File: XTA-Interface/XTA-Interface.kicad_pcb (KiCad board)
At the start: 2 copper layers, 99.9 x 99.9 mm, 23 parts, among them J1 IDE_CONNECTOR, J2 CF Adapter Power, J3 Bus_ISA_8bit, J4 Addresses, J5 Addresses, U1 BIOS FLASH, U2 74HCT245, U3 ATF/GAL22V10x-15, U4 DS1315, U5 AS6C4008-55PCN, Y1 32.768 KHz

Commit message: WIP on XTA interface card.
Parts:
- removed BAT1: CR2032, Battery:BatteryHolder_Keystone_103_1x20mm
- removed C7: 22uF, Capacitor_THT:CP_Radial_D5.0mm_P2.50mm
- removed H1, H3: MountingHole_Pad, MountingHole:MountingHole_3.5mm_Pad
- removed Y1: 32.768 KHz, Crystal:Crystal_C38-LF_D3.0mm_L8.0mm_Horizontal
- added J6: LEDs, Connector_PinHeader_2.54mm:PinHeader_1x04_P2.54mm_Horizontal, F.Cu at (108.6, 52.7)
- added J7: XTA_CONNECTOR_1, Connector_PinHeader_2.54mm:PinHeader_2x20_P2.54mm_Vertical, F.Cu at (123.8, 60.3)
- added R1: 1K, Resistor_SMD:R_1206_3216Metric, F.Cu at (112.4, 52.1)
- C1, C2, C3, C4, C5: footprint Capacitor_THT:C_Disc_D6.0mm_W2.5mm_P5.00mm -> Capacitor_SMD:C_1206_3216Metric
- C6: value 0.1uF -> 22uF 25v; footprint Capacitor_THT:C_Disc_D6.0mm_W2.5mm_P5.00mm -> Capacitor_Tantalum_SMD:CP_EIA-3528-15_AVX-H
- J1: value IDE_CONNECTOR -> XTA_CONNECTOR_0; footprint Connector_PinSocket_2.54mm:PinSocket_2x20_P2.54mm_Vertical -> Connector_PinHeader_2.54mm:PinHeader_2x20_P2.54mm_Vertical
- J2: value CF Adapter Power -> Drive Power; footprint Connector_PinSocket_2.54mm:PinSocket_1x02_P2.54mm_Vertical -> Connector_PinHeader_2.54mm:PinHeader_1x06_P2.54mm_Horizontal
- U4: value DS1315 -> 74LS14; footprint Package_DIP:DIP-16_W7.62mm_Socket -> Package_DIP:DIP-14_W7.62mm_Socket
- U5: value AS6C4008-55PCN -> 74LS00; footprint Package_DIP:DIP-32_W15.24mm_Socket -> Package_DIP:DIP-14_W7.62mm_Socket
- moved J2 98.7 mm to (108.0, 125.1), turned to 180 degrees
- moved C5 73.7 mm to (174.6, 84.5), turned to 0 degrees
- moved J1 71.6 mm to (123.8, 49.5), turned to 90 degrees
- moved U5 69.5 mm to (173.4, 95.2)
- moved C6 63.6 mm to (179.7, 123.2)
- moved C4 56.8 mm to (169.5, 69.2), turned to 0 degrees
- moved U4 53.4 mm to (168.3, 80.0)
- moved C2 44.2 mm to (144.8, 103.5), turned to 180 degrees
- moved C3 35.2 mm to (102.9, 95.9), turned to 0 degrees
- moved H2 22.5 mm to (192.4, 73.7)
- moved H4 13.5 mm to (192.4, 130.2)
- moved U3 13.4 mm to (102.2, 106.7)
- moved U2 11.1 mm to (146.7, 114.3)
- moved U1 6.63 mm to (102.2, 88.9)
- moved C1 3.70 mm to (102.9, 70.5), turned to 0 degrees
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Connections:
- net ROM_ADDR_JUMPER renamed ROM_ADDR_JUMPER_0
- J1 pad 1: ~RESET -> RESET
- J1 pad 10: Net-(J1-Pad10) -> GND
- J1 pad 11: D3_BUF -> D3
- J1 pad 12: Net-(J1-Pad12) -> GND
- J1 pad 13: D2_BUF -> D2
- J1 pad 14: Net-(J1-Pad14) -> GND
- J1 pad 15: D1_BUF -> D1
- J1 pad 16: Net-(J1-Pad16) -> GND
- J1 pad 17: D0_BUF -> D0
- J1 pad 18: Net-(J1-Pad18) -> GND
- J1 pad 21: Net-(J1-Pad21) -> AEN
- J1 pad 25: ~IOR~_DELAYED -> ~IOR
- J1 pad 27: Net-(J1-Pad27) -> ~XTA_DACK
- J1 pad 28: Net-(J1-Pad28) -> GND
- J1 pad 29: VCC -> XTA_DRQ
- J1 pad 3: D7_BUF -> D7
- J1 pad 31: Net-(J1-Pad31) -> XTA_IRQ
- J1 pad 32: Net-(J1-Pad32) -> GND
- J1 pad 33: A02 -> A01
- J1 pad 35: A01 -> A00
- J1 pad 36: A03 -> GND
- J1 pad 37: ~CS1~_ATA -> ~CS_XTA0
- J1 pad 38: VCC -> GND
- J1 pad 39: Net-(J1-Pad39) -> ~DRV_ACTIVE
- J1 pad 4: Net-(J1-Pad4) -> GND
- J1 pad 5: D6_BUF -> D6
- J1 pad 6: Net-(J1-Pad6) -> GND
- J1 pad 7: D5_BUF -> D5
- J1 pad 8: Net-(J1-Pad8) -> GND
- J1 pad 9: D4_BUF -> D4
- J3 pad 15: Net-(J3-Pad15) -> ~DACK3
- J3 pad 16: Net-(J3-Pad16) -> XTA_DRQ
- J3 pad 23: Net-(J3-Pad23) -> IRQ5
- J3 pad 4: Net-(J3-Pad4) -> IRQ2
- J3 pad 42: Net-(J3-Pad42) -> AEN
- J3 pad 9: Net-(J3-Pad9) -> +12V
- J4 pad 4: ATA_ADDR_JUMPER -> ROM_ADDR_JUMPER_1
- J5 pad 2: ~CE~_BIOS_DECODE -> IRQ2
- J5 pad 3: V20_JUMPER -> BIOS_SEL_JUMPER
- J5 pad 4: ~CE~_BIOS -> XTA_IRQ
- J5 pad 6: ~CE~_BIOS_THRU -> IRQ5
- U1 pad 2: V20_JUMPER -> GND
- U1 pad 28: A13 -> BIOS_SEL_JUMPER
- U1 pad 29: A14 -> GND
- U1 pad 3: ATA_ADDR_JUMPER -> GND
- U2 pad 1: ~IOR_OR_MEMR -> ~MEMR
- U2 pad 19: GND -> ~CE~_BIOS
- U3 pad 1: A04 -> A02
- U3 pad 10: A17 -> A14
- U3 pad 11: A18 -> A15
- U3 pad 13: A19 -> A16
- U3 pad 14: ~IOR~_DELAYED -> A17
- U3 pad 15: ~IOR_OR_MEMR -> A18
- U3 pad 16: ~MEMR~_DELAYED -> A19
- U3 pad 18: ~CE~_BIOS_DECODE -> ~MEMR~_DELAYED
- U3 pad 19: ~CS1~_ATA -> ~CE~_BIOS
- U3 pad 2: A05 -> A03
- U3 pad 20: ~RESET -> ~CS_XTA0
- U3 pad 21: ~IOR -> ~CS_XTA1
- U3 pad 22: ATA_ADDR_JUMPER -> ROM_ADDR_JUMPER_1
- U3 pad 3: A06 -> A04
- U3 pad 4: A07 -> A05
- U3 pad 5: A08 -> A06
- U3 pad 6: A09 -> A07
- U3 pad 7: RESET -> A08
- U3 pad 8: A15 -> A09
- U3 pad 9: A16 -> A13
- U4 pad 1: /XTAL1 -> Net-(U4-Pad1)
- U4 pad 10: ~CE~_BIOS_THRU -> Net-(U4-Pad10)
- U4 pad 11: ~CE~_BIOS_DECODE -> Net-(U4-Pad11)
- U4 pad 12: ~MEMR~_DELAYED -> Net-(U4-Pad12)
- U4 pad 13: VCC -> Net-(U4-Pad13)
- U4 pad 14: GND -> VCC
- U4 pad 2: /XTAL2 -> Net-(U4-Pad2)
- U4 pad 3: A02 -> Net-(U4-Pad3)
- U4 pad 4: Net-(BAT1-Pad1) -> Net-(U4-Pad4)
- U4 pad 5: GND -> Net-(U4-Pad4)
- U4 pad 6: A00 -> Net-(U4-Pad6)
- U4 pad 7: D0_BUF -> GND
- U4 pad 8: GND -> Net-(U4-Pad8)
- U4 pad 9: Net-(U4-Pad15) -> Net-(U4-Pad6)
- U5 pad 1: A18 -> ~IOR
- U5 pad 10: A02 -> Net-(U5-Pad10)
- U5 pad 11: A01 -> Net-(U5-Pad10)
- U5 pad 12: A00 -> ~DACK3
- U5 pad 13: D0_BUF -> Net-(U4-Pad8)
- U5 pad 14: D1_BUF -> VCC
- U5 pad 2: A16 -> ~IOW
- U5 pad 3: A14 -> Net-(U4-Pad3)
- U5 pad 4: A12 -> ~DACK3
- U5 pad 5: A07 -> ~XTA_DACK
- U5 pad 6: A06 -> Net-(U5-Pad6)
- U5 pad 7: A05 -> GND
- U5 pad 8: A04 -> ~XTA_DACK
- U5 pad 9: A03 -> Net-(U5-Pad6)
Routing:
- net VCC: track 458.0 -> 263.2 mm, vias 7 -> 4
- net A02: track 145.1 -> 12.1 mm, vias 3 -> 0
- net A03: track 136.2 -> 11.6 mm, vias 4 -> 0
- net ~MEMW: track 127.6 -> 5.78 mm, vias 5 -> 1
- net A10: track 123.0 -> 7.14 mm, vias 3 -> 0
- net A01: track 133.6 -> 25.1 mm, vias 3 -> 0
- net D7: track 29.0 -> 128.2 mm, vias 0 -> 1
- net ~CS1~_ATA: track 96.9 -> 0.00 mm, vias 2 -> 0
- net A11: track 108.8 -> 12.3 mm, vias 4 -> 0
- net D6: track 27.7 -> 123.7 mm, vias 0 -> 1
- net D5: track 27.7 -> 120.5 mm, vias 0 -> 1
- net ~CE~_BIOS_DECODE: track 89.3 -> 0.00 mm, vias 4 -> 0
- net A13: track 97.2 -> 9.68 mm, vias 2 -> 0
- net D4: track 27.3 -> 113.3 mm, vias 0 -> 1
- net D3: track 27.0 -> 111.4 mm, vias 0 -> 1
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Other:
- board text added: "BIOS"
- board text added: "IRQ"
- board text added: "ROM ADDR 0"
- board text added: "ROM ADDR 1"
- board text added: "v1.0"
- board text removed: "6pF"
- board text removed: "Compact Flash with XT-IDE BIOS"
- board text removed: "Compact Flash with XT-IDE BIOS and SmartWatch"
- board text removed: "Compact Flash with XT-IDE BIOS, SmartWatch and 512K SRAM. For original Tandy 1000, 1000A or 1000 HD only. Remove any other RAM upgrade before installing."
- board text removed: "In memory of my father, Michael James Lee-Steere. Our early experiences with the Tandy 1000 provided the inspiration for creating this upgrade."
- board text removed: "KEYSTONE 103 OR SIMILAR"
- board text removed: "USE CR2032"
- board text removed: "v1.1"

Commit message: WIP on XTA interface card.
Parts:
- removed the C5 at (174.6, 84.5)
- removed U5: 74LS00, Package_DIP:DIP-14_W7.62mm_Socket
- U3: value ATF/GAL22V10x-15 -> ATF/GAL16V8-15; footprint Package_DIP:DIP-24_W7.62mm_Socket -> Package_DIP:DIP-20_W7.62mm_Socket
- U4: value 74LS14 -> ATF/GAL16V8-15; footprint Package_DIP:DIP-14_W7.62mm_Socket -> Package_DIP:DIP-20_W7.62mm_Socket
- moved C4 83.7 mm to (87.0, 83.2)
- moved U4 59.7 mm to (116.2, 109.2)
- moved C2 57.9 mm to (87.0, 100.3)
- moved U3 57.2 mm to (159.4, 109.2)
- moved J4 44.7 mm to (102.2, 101.9)
- moved J5 44.7 mm to (108.6, 101.9)
- moved U2 28.4 mm to (159.4, 88.9)
- moved C3 15.9 mm to (87.0, 95.2)
- moved J2 0.64 mm to (108.0, 124.5)
- renumbered C6 to C5
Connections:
- J2 pad 1: VCC -> +12V
- J2 pad 3: Net-(J2-Pad3) -> VCC
- J2 pad 4: GND -> VCC
- J2 pad 5: +12V -> GND
- J4 pad 3: ROM_ADDR_JUMPER_0 -> ADDR_JUMPER_0
- J4 pad 4: ROM_ADDR_JUMPER_1 -> ADDR_JUMPER_1
- J5 pad 3: BIOS_SEL_JUMPER -> ST_WD_JUMPER
- U1 pad 28: BIOS_SEL_JUMPER -> ST_WD_JUMPER
- U3 pad 1: A02 -> DECODE_IO_RANGE
- U3 pad 10: A14 -> GND
- U3 pad 11: A15 -> A19
- U3 pad 12: GND -> Net-(U3-Pad12)
- U3 pad 13: A16 -> ~MEMR
- U3 pad 14: A17 -> ~MEMR~_DELAYED
- U3 pad 15: A18 -> ~CE~_BIOS
- U3 pad 16: A19 -> ~CS_XTA0
- U3 pad 17: ~MEMR -> ~CS_XTA1
- U3 pad 18: ~MEMR~_DELAYED -> ADDR_JUMPER_1
- U3 pad 19: ~CE~_BIOS -> ADDR_JUMPER_0
- U3 pad 2: A03 -> ST_WD_JUMPER
- U3 pad 20: ~CS_XTA0 -> VCC
- U3 pad 3: A04 -> A02
- U3 pad 4: A05 -> A13
- U3 pad 5: A06 -> A14
- U3 pad 6: A07 -> A15
- U3 pad 7: A08 -> A16
- U3 pad 8: A09 -> A17
- U3 pad 9: A13 -> A18
- U4 pad 1: Net-(U4-Pad1) -> A03
- U4 pad 10: Net-(U4-Pad10) -> GND
- U4 pad 11: Net-(U4-Pad11) -> ~DACK3
- U4 pad 12: Net-(U4-Pad12) -> ~XTA_DACK
- U4 pad 13: Net-(U4-Pad13) -> DECODE_IO_RANGE
- U4 pad 14: VCC -> Net-(U4-Pad14)
- U4 pad 2: Net-(U4-Pad2) -> A04
- U4 pad 3: Net-(U4-Pad3) -> A05
- U4 pad 4: Net-(U4-Pad4) -> A06
- U4 pad 5: Net-(U4-Pad4) -> A07
- U4 pad 6: Net-(U4-Pad6) -> A08
- U4 pad 7: GND -> A09
- U4 pad 8: Net-(U4-Pad8) -> ~IOW
- U4 pad 9: Net-(U4-Pad6) -> ~IOR
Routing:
- net GND: track 340.7 -> 445.1 mm, vias 17 -> 38
- net VCC: track 263.2 -> 219.1 mm, vias 4 -> 2
- net D0_BUF: track 41.6 -> 0.00 mm, vias 1 -> 0
- net D1_BUF: track 39.8 -> 0.00 mm, vias 1 -> 0
- net D2_BUF: track 38.0 -> 0.00 mm, vias 1 -> 0
- net ~CE~_BIOS: track 33.0 -> 0.00 mm
- net D7: track 128.2 -> 96.1 mm
- net D6: track 123.7 -> 95.4 mm
- net D5: track 120.5 -> 93.4 mm
- net D3: track 111.4 -> 84.7 mm
- net D2: track 105.6 -> 80.3 mm
- net D1: track 100.5 -> 75.8 mm
- net D4: track 113.3 -> 89.1 mm
- net D0: track 94.5 -> 72.0 mm, vias 0 -> 1
- net D3_BUF: track 50.6 -> 39.7 mm
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
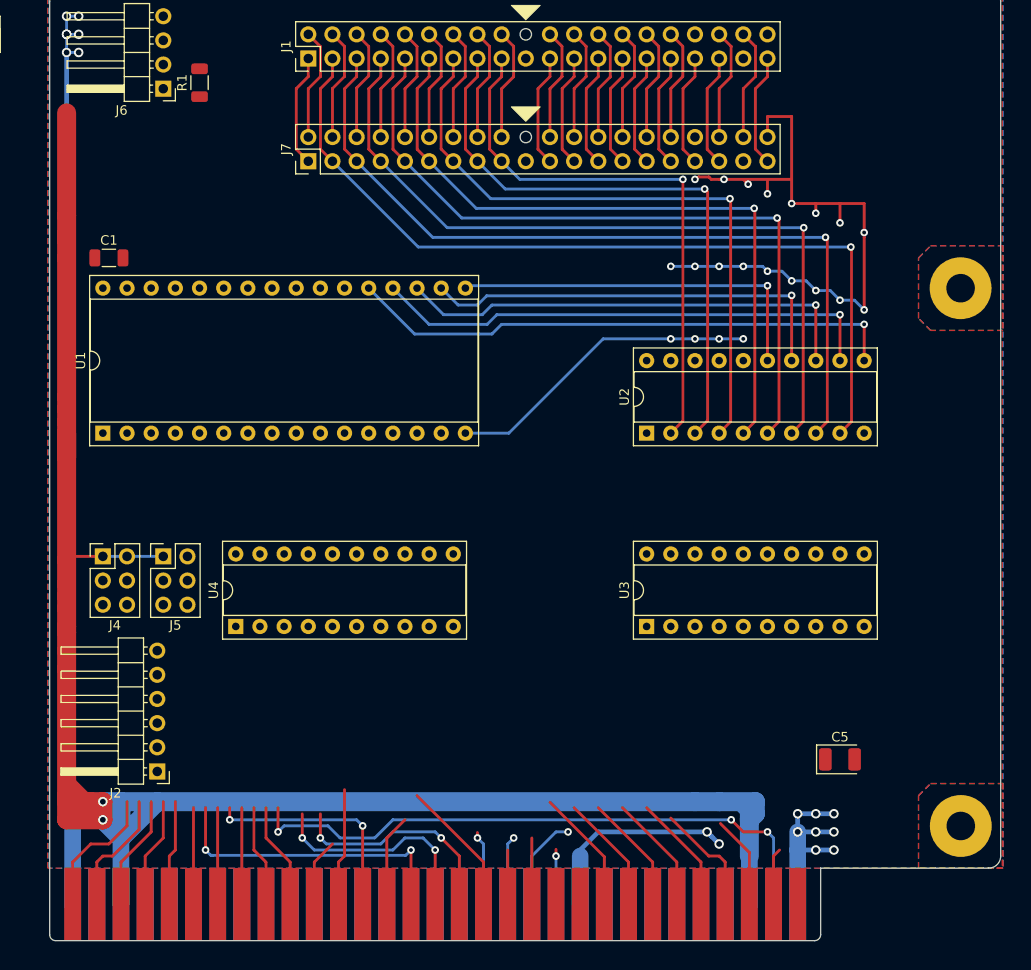
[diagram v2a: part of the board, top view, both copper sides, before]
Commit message: More WIP on XTA interface card.
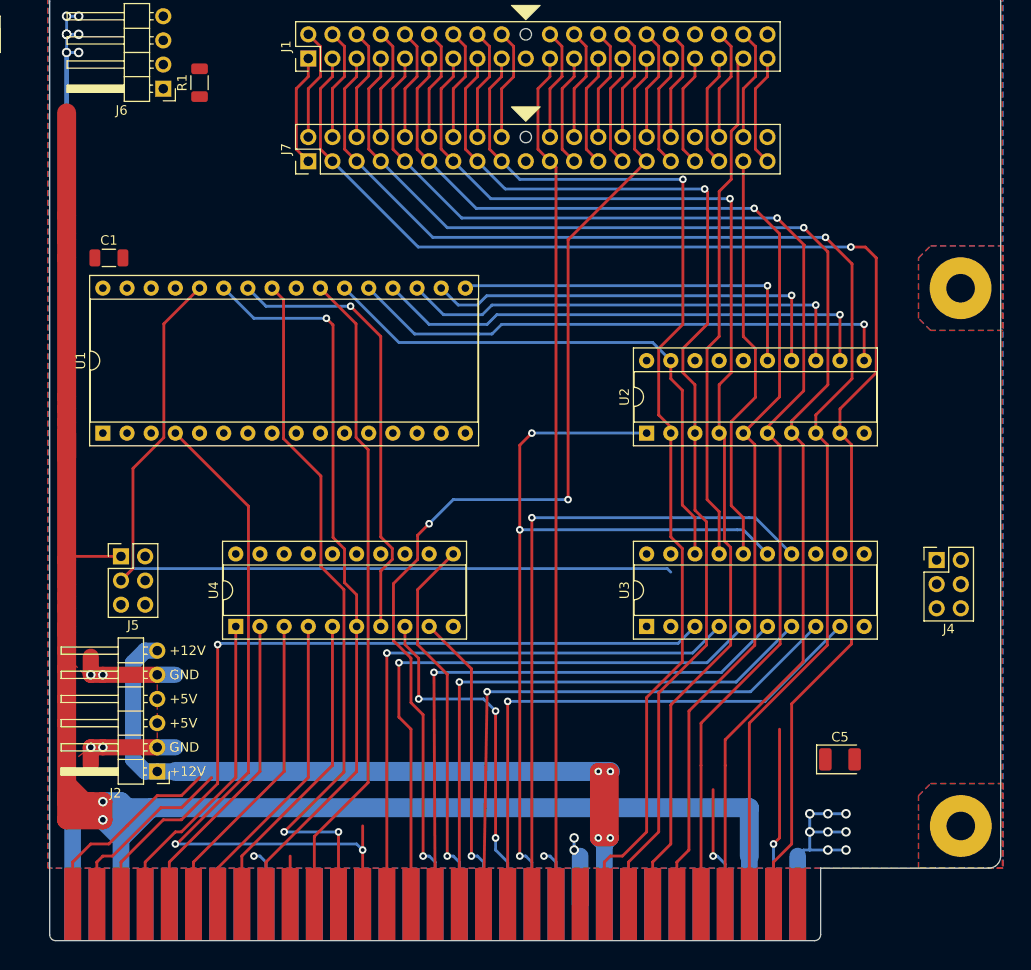
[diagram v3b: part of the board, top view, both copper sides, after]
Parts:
- moved J4 87.6 mm to (189.9, 102.2)
- moved J5 4.44 mm to (104.1, 101.9)
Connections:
- net XTA_DRQ renamed DRQ3
- U3 pad 11: A19 -> ADDR_JUMPER_0
- U3 pad 12: Net-(U3-Pad12) -> ADDR_JUMPER_1
- U3 pad 13: ~MEMR -> Net-(U3-Pad13)
- U3 pad 14: ~MEMR~_DELAYED -> A19
- U3 pad 15: ~CE~_BIOS -> ~MEMR
- U3 pad 16: ~CS_XTA0 -> ~CS_XTA1
- U3 pad 17: ~CS_XTA1 -> ~CS_XTA0
- U3 pad 18: ADDR_JUMPER_1 -> ~CE~_BIOS
- U3 pad 19: ADDR_JUMPER_0 -> ~MEMR~_DELAYED
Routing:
- net DRQ3: track 11.8 -> 110.2 mm, vias 0 -> 3
- net GND: track 445.1 -> 349.5 mm, vias 38 -> 21
- net ST_WD_JUMPER: track 0.00 -> 92.6 mm
- net +12V: track 0.00 -> 90.1 mm, vias 0 -> 4
- net ~MEMR: track 9.94 -> 90.1 mm, vias 1 -> 3
- net AEN: track 11.8 -> 90.2 mm
- net A02: track 12.1 -> 83.6 mm, vias 0 -> 1
- net A08: track 10.7 -> 79.0 mm, vias 0 -> 1
- net A11: track 12.3 -> 76.2 mm, vias 0 -> 2
- net A19: track 6.99 -> 69.5 mm, vias 0 -> 1
- net A10: track 7.14 -> 69.2 mm
- net ~CE~_BIOS: track 0.00 -> 58.8 mm
- net ~CS_XTA0: track 0.00 -> 54.2 mm
- net A12: track 23.8 -> 77.8 mm
- net A18: track 5.72 -> 59.5 mm, vias 0 -> 1
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- added copper zone on F.Cu, net VCC
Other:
- board text added: "+12V"
- board text added: "+5V"
- board text added: "GND"

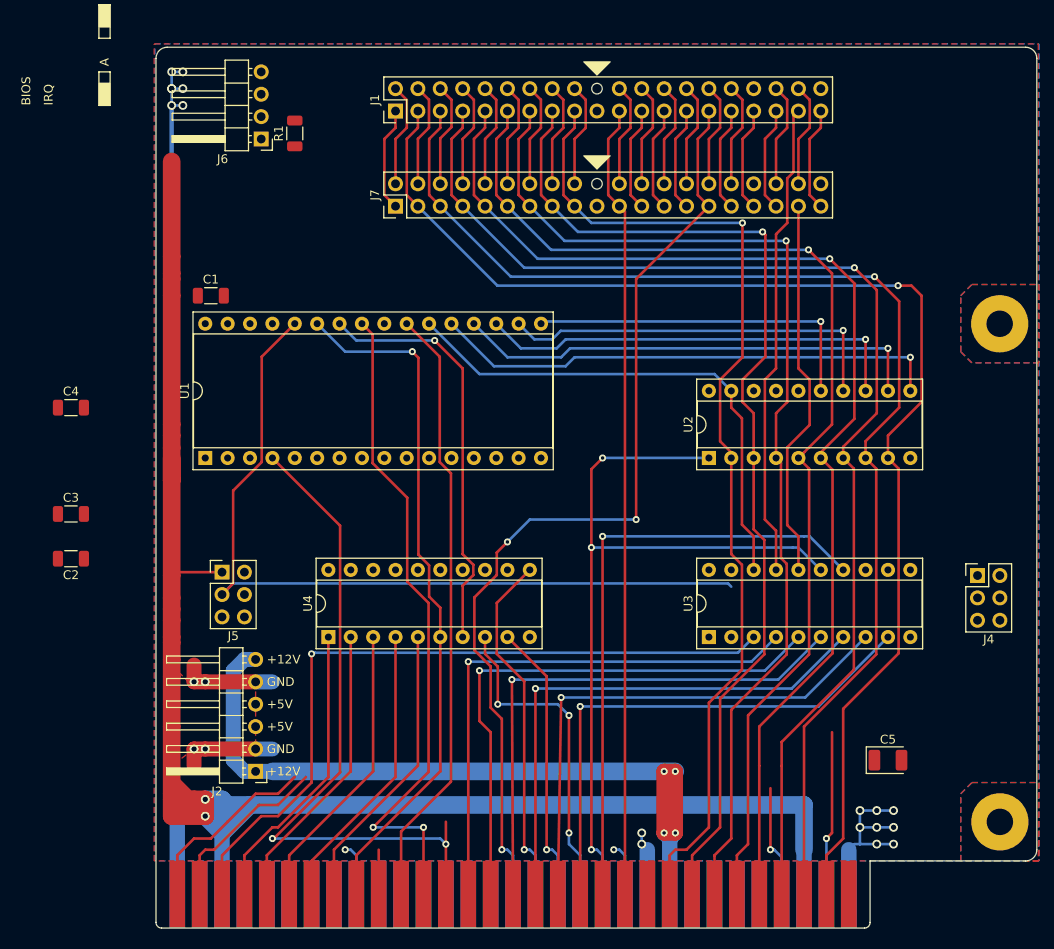
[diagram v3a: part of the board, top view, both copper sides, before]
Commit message: XTA interface WIP. All items connected - still needs a bunch of cleanup.
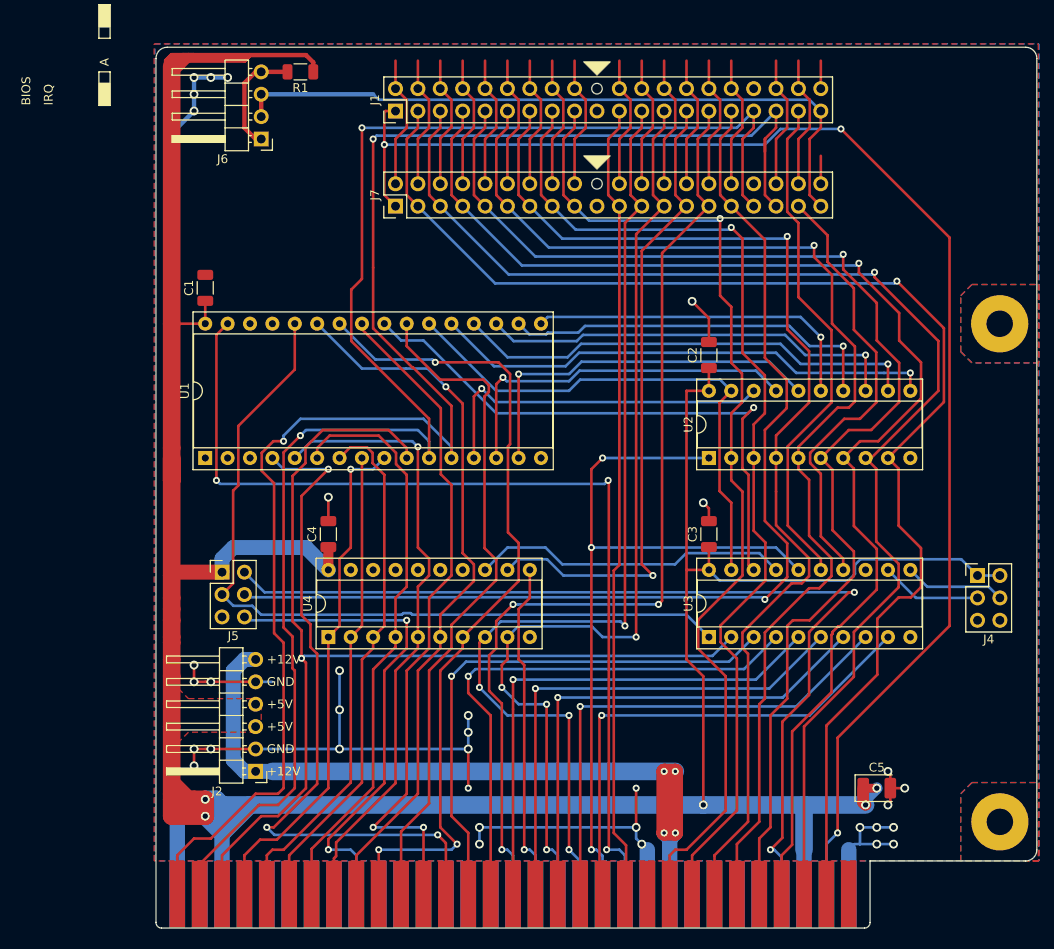
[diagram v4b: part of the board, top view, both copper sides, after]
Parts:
- moved C2 76.0 mm to (159.4, 77.2), turned to 90 degrees
- moved C3 72.4 mm to (159.4, 97.5), turned to 90 degrees
- moved C4 32.5 mm to (116.2, 97.5), turned to 90 degrees
- moved R1 7.01 mm to (113.0, 45.1), turned to 180 degrees
- moved C5 3.42 mm to (178.4, 126.4)
- moved C1 1.09 mm to (102.2, 69.6), turned to 90 degrees
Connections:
- U3 pad 1: DECODE_IO_RANGE -> ST_WD_JUMPER
- U3 pad 11: ADDR_JUMPER_0 -> ADDR_JUMPER_1
- U3 pad 12: ADDR_JUMPER_1 -> ADDR_JUMPER_0
- U3 pad 14: A19 -> ~CS_XTA1
- U3 pad 15: ~MEMR -> ~CS_XTA0
- U3 pad 16: ~CS_XTA1 -> ~MEMR
- U3 pad 17: ~CS_XTA0 -> DECODE_IO_RANGE
- U3 pad 18: ~CE~_BIOS -> ~MEMR~_DELAYED
- U3 pad 19: ~MEMR~_DELAYED -> ~CE~_BIOS
- U3 pad 2: ST_WD_JUMPER -> A02
- U3 pad 3: A02 -> A13
- U3 pad 4: A13 -> A14
- U3 pad 5: A14 -> A15
- U3 pad 6: A15 -> A16
- U3 pad 7: A16 -> A17
- U3 pad 8: A17 -> A18
- U3 pad 9: A18 -> A19
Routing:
- net VCC: track 201.1 -> 389.5 mm, vias 2 -> 5
- net A00: track 33.3 -> 185.1 mm, vias 0 -> 2
- net A01: track 32.0 -> 175.1 mm, vias 0 -> 2
- net GND: track 349.5 -> 485.0 mm, vias 21 -> 34
- net RESET: track 30.5 -> 162.8 mm, vias 1 -> 3
- net XTA_IRQ: track 11.8 -> 121.5 mm, vias 0 -> 1
- net ~MEMW: track 5.98 -> 111.9 mm, vias 1 -> 3
- net IRQ2: track 12.8 -> 109.5 mm, vias 1 -> 2
- net ~IOR: track 43.8 -> 112.0 mm, vias 1 -> 4
- net ~DRV_ACTIVE: track 11.8 -> 78.7 mm
- net ~IOW: track 49.5 -> 115.4 mm, vias 3 -> 4
- net ~MEMR~_DELAYED: track 0.00 -> 65.8 mm, vias 0 -> 1
- net ~XTA_DACK: track 11.8 -> 74.2 mm, vias 0 -> 1
- net IRQ5: track 5.98 -> 56.2 mm, vias 1 -> 2
- net D2_BUF: track 0.00 -> 43.2 mm, vias 0 -> 1
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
